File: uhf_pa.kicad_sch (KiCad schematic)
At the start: 26 parts, among them U12 FPF2701, U13 TQP7M9106

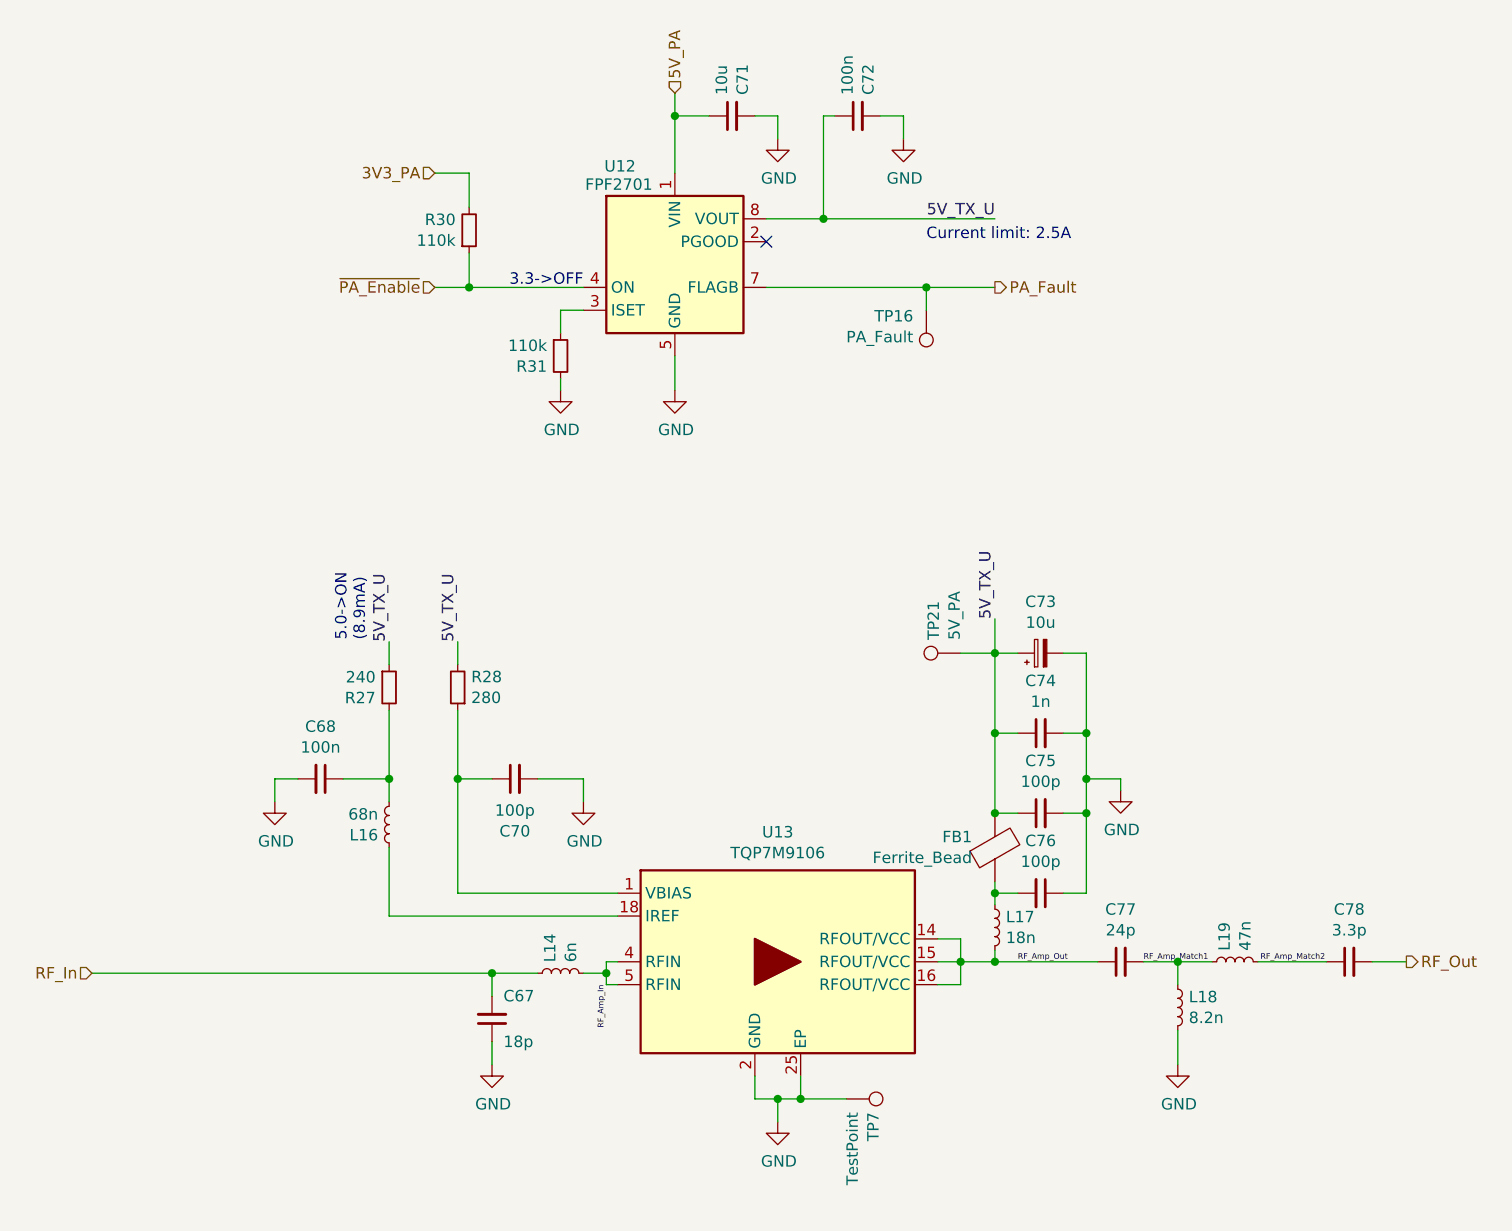
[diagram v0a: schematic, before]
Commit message: feat: layout changed for new RF part
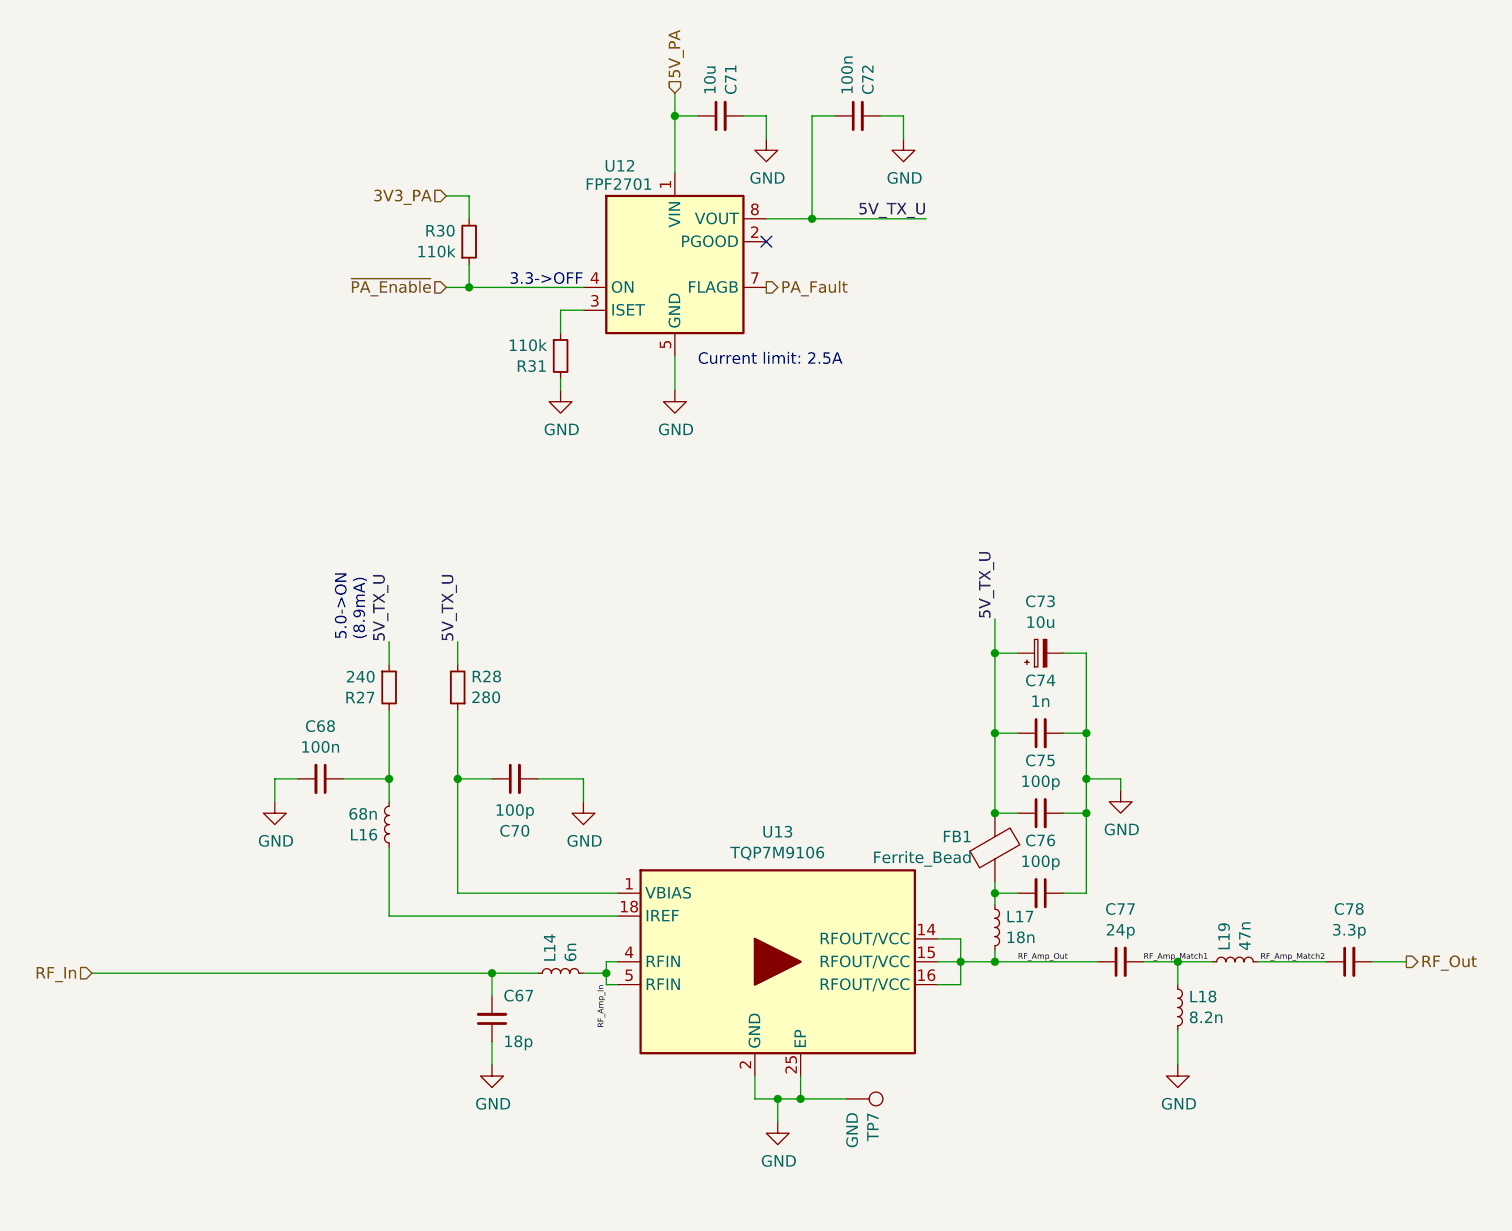
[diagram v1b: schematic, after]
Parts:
- removed TP16: PA_Fault, lsf-kicad-lib:TestPoint_D0.8mm_Mask-Only, symbol Connector:TestPoint
- removed TP21: 5V_PA, lsf-kicad-lib:TestPoint_D0.8mm_Mask-Only, symbol Connector:TestPoint
- TP7: value TestPoint -> GND
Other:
- moved on the sheet: C71, R30

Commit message: feat(RF): better LPF tuning and add part numbers to all inductors
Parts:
- L14: Mnf. TDK -> (none); PartNumber MHQ1005P68NGTD25 -> LQW15AN6N0B80D
- L16: Mnf. Coilcraft -> (none); PartNumber 0402DC-68NXJRW -> LQW15AN68NJ0ZD
- L17: Mnf. Coilcraft -> (none)
- L18: Mnf. TDK -> (none); PartNumber MHQ1005P8N2GT000 -> LQW15AN8N2H00D
- L19: Mnf. ABRACON -> (none); PartNumber AISC-0402-47NG-T -> LQW15AN47NJ8ZD
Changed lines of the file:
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@@
-      (effects (font (size 1.27 1.27)) hide)
-    )
-    (property "Mnf." "Coilcraft" (id 5) (at 175.26 123.19 0)
-      (effects (font (size 1.27 1.27)) hide)
-    )
-    (property "Description" "Inductor, 0805, 5%, Coilcraft CS Series" (id 6) (at 175.26 123.19 0)
       (effects (font (size 1.27 1.27)) hide)
     )
@@
       (effects (font (size 1.27 1.27)) hide)
     )
-    (property "Mnf." "ABRACON" (id 4) (at 201.93 127 0)
-      (effects (font (size 1.27 1.27)) hide)
-    )
-    (property "PartNumber" "AISC-0402-47NG-T" (id 5) (at 201.93 127 0)
+    (property "PartNumber" "LQW15AN47NJ8ZD" (id 4) (at 201.93 127 0)
       (effects (font (size 1.27 1.27)) hide)
     )
@@
       (effects (font (size 1.27 1.27)) hide)
     )
-    (property "Description" "Inductor, 0603, 5%, Ceramic" (id 4) (at 107.95 111.76 0)
-      (effects (font (size 1.27 1.27)) hide)
-    )
-    (property "Mnf." "Coilcraft" (id 5) (at 107.95 111.76 0)
-      (effects (font (size 1.27 1.27)) hide)
-    )
-    (property "PartNumber" "0402DC-68NXJRW" (id 6) (at 107.95 111.76 0)
+    (property "PartNumber" "LQW15AN68NJ0ZD" (id 6) (at 107.95 111.76 0)
       (effects (font (size 1.27 1.27)) hide)
     )
@@
       (effects (font (size 1.27 1.27)) hide)
     )
-    (property "Mnf." "TDK" (id 4) (at 127 128.27 0)
-      (effects (font (size 1.27 1.27)) hide)
-    )
-    (property "PartNumber" "MHQ1005P68NGTD25" (id 5) (at 127 128.27 0)
+    (property "PartNumber" "LQW15AN6N0B80D" (id 4) (at 127 128.27 0)
       (effects (font (size 1.27 1.27)) hide)
     )
@@
       (effects (font (size 1.27 1.27)) hide)
     )
-    (property "Mnf." "TDK" (id 4) (at 195.58 132.08 0)
-      (effects (font (size 1.27 1.27)) hide)
-    )
-    (property "PartNumber" "MHQ1005P8N2GT000" (id 5) (at 195.58 132.08 0)
-      (effects (font (size 1.27 1.27)) hide)
-    )
+    (property "PartNumber" "LQW15AN8N2H00D" (id 4) (at 195.58 132.08 0)
+      (effects (font (size 1.27 1.27)) hide)
+    )

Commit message: Fix mismatch between footprint and part number for C48, C72, C74, R13, R24, R21, R27, R28, R30, R31
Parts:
- C72: Mnf. KEMET -> (none); PartNumber C0402C104K4RACTU -> (none)
- C74: Mnf. KEMET -> (none); PartNumber C0402C102K5GECAUTO7411 -> (none)
- R27: Mnf. Vishay -> (none); PartNumber CRCW0402240RFKEDC -> (none)
- R28: Mnf. YAGEO -> (none); PartNumber RC0402FR-07280RL -> (none)
- R30: PartNumber CR0402-FX-1003GLF -> (none)
- R31: Mnf. Vishay -> (none); PartNumber CRCW0402110KFKED -> (none)
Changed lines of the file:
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@@
       (effects (font (size 1.27 1.27)) hide)
     )
-    (property "Description" "Capacitor, 0603, 10%, 50V, NPO/COG" (id 4) (at 180.34 101.6 90)
-      (effects (font (size 1.27 1.27)) hide)
-    )
-    (property "Mnf." "KEMET" (id 5) (at 180.34 101.6 0)
-      (effects (font (size 1.27 1.27)) hide)
-    )
-    (property "PartNumber" "C0402C102K5GECAUTO7411" (id 6) (at 180.34 101.6 0)
+    (property "Description" "" (id 4) (at 180.34 101.6 90)
+      (effects (font (size 1.27 1.27)) hide)
+    )
+    (property "Mnf." "" (id 5) (at 180.34 101.6 0)
+      (effects (font (size 1.27 1.27)) hide)
+    )
+    (property "PartNumber" "" (id 6) (at 180.34 101.6 0)
       (effects (font (size 1.27 1.27)) hide)
     )
@@
       (effects (font (size 1.27 1.27)) hide)
     )
-    (property "Mnf." "YAGEO" (id 5) (at 115.57 96.52 0)
-      (effects (font (size 1.27 1.27)) hide)
-    )
-    (property "PartNumber" "RC0402FR-07280RL" (id 6) (at 115.57 96.52 0)
+    (property "Mnf." "" (id 5) (at 115.57 96.52 0)
+      (effects (font (size 1.27 1.27)) hide)
+    )
+    (property "PartNumber" "" (id 6) (at 115.57 96.52 0)
       (effects (font (size 1.27 1.27)) hide)
     )
@@
       (effects (font (size 1.27 1.27)) hide)
     )
-    (property "Mnf." "Vishay" (id 5) (at 107.95 96.52 0)
-      (effects (font (size 1.27 1.27)) hide)
-    )
-    (property "PartNumber" "CRCW0402240RFKEDC" (id 6) (at 107.95 96.52 0)
+    (property "Mnf." "" (id 5) (at 107.95 96.52 0)
+      (effects (font (size 1.27 1.27)) hide)
+    )
+    (property "PartNumber" "" (id 6) (at 107.95 96.52 0)
       (effects (font (size 1.27 1.27)) hide)
     )
@@
       (effects (font (size 1.27 1.27)) hide)
     )
-    (property "Description" "Resistor, 0402, 5%, 1/16W" (id 4) (at 116.84 46.99 0)
+    (property "Description" "" (id 4) (at 116.84 46.99 0)
       (effects (font (size 1.27 1.27)) hide)
     )
@@
       (effects (font (size 1.27 1.27)) hide)
     )
-    (property "PartNumber" "CR0402-FX-1003GLF" (id 6) (at 116.84 46.99 0)
+    (property "PartNumber" "" (id 6) (at 116.84 46.99 0)
       (effects (font (size 1.27 1.27)) hide)
     )
@@
       (effects (font (size 1.27 1.27)) hide)
     )
-    (property "Description" "Resistor, 0402, 1%, 1/16W" (id 4) (at 127 59.69 0)
-      (effects (font (size 1.27 1.27)) hide)
-    )
-    (property "Mnf." "Vishay" (id 5) (at 127 59.69 0)
-      (effects (font (size 1.27 1.27)) hide)
-    )
-    (property "PartNumber" "CRCW0402110KFKED" (id 6) (at 127 59.69 0)
+    (property "Description" "" (id 4) (at 127 59.69 0)
+      (effects (font (size 1.27 1.27)) hide)
+    )
+    (property "Mnf." "" (id 5) (at 127 59.69 0)
+      (effects (font (size 1.27 1.27)) hide)
+    )
+    (property "PartNumber" "" (id 6) (at 127 59.69 0)
       (effects (font (size 1.27 1.27)) hide)
     )
@@
       (effects (font (size 1.27 1.27)) hide)
     )
-    (property "Description" "Capacitor, 0603, 10%, 50V, X7R" (id 4) (at 160.02 33.02 0)
-      (effects (font (size 1.27 1.27)) hide)
-    )
-    (property "Mnf." "KEMET" (id 5) (at 160.02 33.02 0)
-      (effects (font (size 1.27 1.27)) hide)
-    )
-    (property "PartNumber" "C0402C104K4RACTU" (id 6) (at 160.02 33.02 0)
-      (effects (font (size 1.27 1.27)) hide)
-    )
+    (property "Description" "" (id 4) (at 160.02 33.02 0)
+      (effects (font (size 1.27 1.27)) hide)
+    )
+    (property "Mnf." "" (id 5) (at 160.02 33.02 0)
+      (effects (font (size 1.27 1.27)) hide)
+    )
+    (property "PartNumber" "" (id 6) (at 160.02 33.02 0)
+      (effects (font (size 1.27 1.27)) hide)
+    )

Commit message: Update values of components in the RF subsystem and swap CL instead of LC filter (L14 and C67)
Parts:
- C67: value 18p -> 50p
- L14: value 6n -> 4n
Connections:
- net GND: now also L14.1; no longer C67.1
- net RF_Amp_In: now also C67.1; no longer L14.2
- net RF_In: now also L14.2; no longer L14.1
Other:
- moved on the sheet: C67, L14
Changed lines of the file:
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@@
     (pin "2")
   )
-  (symbol (lib_id "Device:L_Small") (at 127 128.27 90) (unit 1)
+  (symbol (lib_id "Device:L_Small") (at 119.38 133.35 180) (unit 1)
     (in_bom yes) (on_board yes)
-    (property "Reference" "L14" (id 0) (at 125.8316 127.0508 0)
+    (property "Reference" "L14" (id 0) (at 118.1608 134.5184 0)
       (effects (font (size 1.27 1.27)) (justify left))
     )
-    (property "Value" "6n" (id 1) (at 128.143 127.0508 0)
+    (property "Value" "4n" (id 1) (at 118.1608 132.207 0)
       (effects (font (size 1.27 1.27)) (justify left))
     )
-    (property "Footprint" "Inductor_SMD:L_0402_1005Metric" (id 2) (at 127 128.27 0)
+    (property "Footprint" "Inductor_SMD:L_0402_1005Metric" (id 2) (at 119.38 133.35 0)
       (effects (font (size 1.27 1.27)) hide)
     )
-    (property "Datasheet" "~" (id 3) (at 127 128.27 0)
+    (property "Datasheet" "~" (id 3) (at 119.38 133.35 0)
       (effects (font (size 1.27 1.27)) hide)
     )
-    (property "PartNumber" "LQW15AN6N0B80D" (id 4) (at 127 128.27 0)
+    (property "PartNumber" "LQW15AN6N0B80D" (id 4) (at 119.38 133.35 0)
       (effects (font (size 1.27 1.27)) hide)
     )
@@
     (pin "2")
   )
-  (symbol (lib_id "Device:C_Small") (at 119.38 133.35 0) (mirror x) (unit 1)
+  (symbol (lib_id "Device:C_Small") (at 127 128.27 270) (mirror x) (unit 1)
     (in_bom yes) (on_board yes)
-    (property "Reference" "C67" (id 0) (at 120.65 130.81 0)
+    (property "Reference" "C67" (id 0) (at 125.73 132.08 90)
       (effects (font (size 1.27 1.27)) (justify left))
     )
-    (property "Value" "18p" (id 1) (at 120.65 135.89 0)
+    (property "Value" "50p" (id 1) (at 125.73 134.62 90)
       (effects (font (size 1.27 1.27)) (justify left))
     )
-    (property "Footprint" "Capacitor_SMD:C_0402_1005Metric" (id 2) (at 119.38 133.35 0)
+    (property "Footprint" "Capacitor_SMD:C_0402_1005Metric" (id 2) (at 127 128.27 0)
       (effects (font (size 1.27 1.27)) hide)
     )
-    (property "Datasheet" "~" (id 3) (at 119.38 133.35 0)
+    (property "Datasheet" "~" (id 3) (at 127 128.27 0)
       (effects (font (size 1.27 1.27)) hide)
     )
-    (property "Mnf." "Murata Electronics" (id 4) (at 119.38 133.35 0)
+    (property "Mnf." "Murata Electronics" (id 4) (at 127 128.27 0)
       (effects (font (size 1.27 1.27)) hide)
     )
-    (property "PartNumber" "GJM1555C1H2R0WB01D" (id 5) (at 119.38 133.35 0)
+    (property "PartNumber" "GJM1555C1H2R0WB01D" (id 5) (at 127 128.27 0)
       (effects (font (size 1.27 1.27)) hide)
     )
